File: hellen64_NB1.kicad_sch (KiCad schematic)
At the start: 192 parts, among them J1 USB_B_Mini, J11 Conn_01x01, J13 Conn_01x01, J14 Conn_01x01, J15 Conn_01x01, J16 Conn_01x01, J17 Conn_01x01, J19 Conn_01x01, J2 Conn_01x05_Male, J20 Conn_01x01, J21 Conn_01x01, J22 Conn_01x01, J24 Conn_01x01, J25 AudioJack3_SwitchTR, J27 Conn_01x06, J3 MiniFit, J4 Conn_02x12_Odd_Even, J5 USB_B, J6 ETB, M1 Module-input-0.1, M10 Module-power12-0.2, M11 Module-power5-0.2, M12 Module-wbo-0.2, M13 Module-can-0.1, M2 Module-ign8-0.1, M3 Module-mcu144-0.5, M4 Module-sd-0.1, M5 Module-output-0.2, M6 Module-dinput4-0.1, M7 Module-stlink-0.1, M8 Module-can-0.1, M9 Module-knock-0.1, P1 Pad, P10 Pad, P11 Pad, P12 Pad, P13 Pad, P14 Pad, P15 Pad, P17 Pad, P18 Pad, P19 Pad, P2 178780-1, P20 Pad, P22 Pad, P23 Pad, P24 Pad, P25 Pad, P28 Pad, P29 Pad, P30 Pad, P31 Pad, P32 Pad, P38 Pad, P4 Pad, P43 Pad, P44 Pad, P47 Pad, P48 Pad, P49 Pad, P5 Pad, P50 Pad, P51 Pad, P52 Pad, P53 Pad, P55 Pad, P56 Pad, P6 Pad, P7 Pad, P8 Pad, P9 Pad, U1 LIS2DW12TR, U2 MPX4_MAP, U3 MCP6002-xSN, U4 LPS25HB, U5 L6205PD

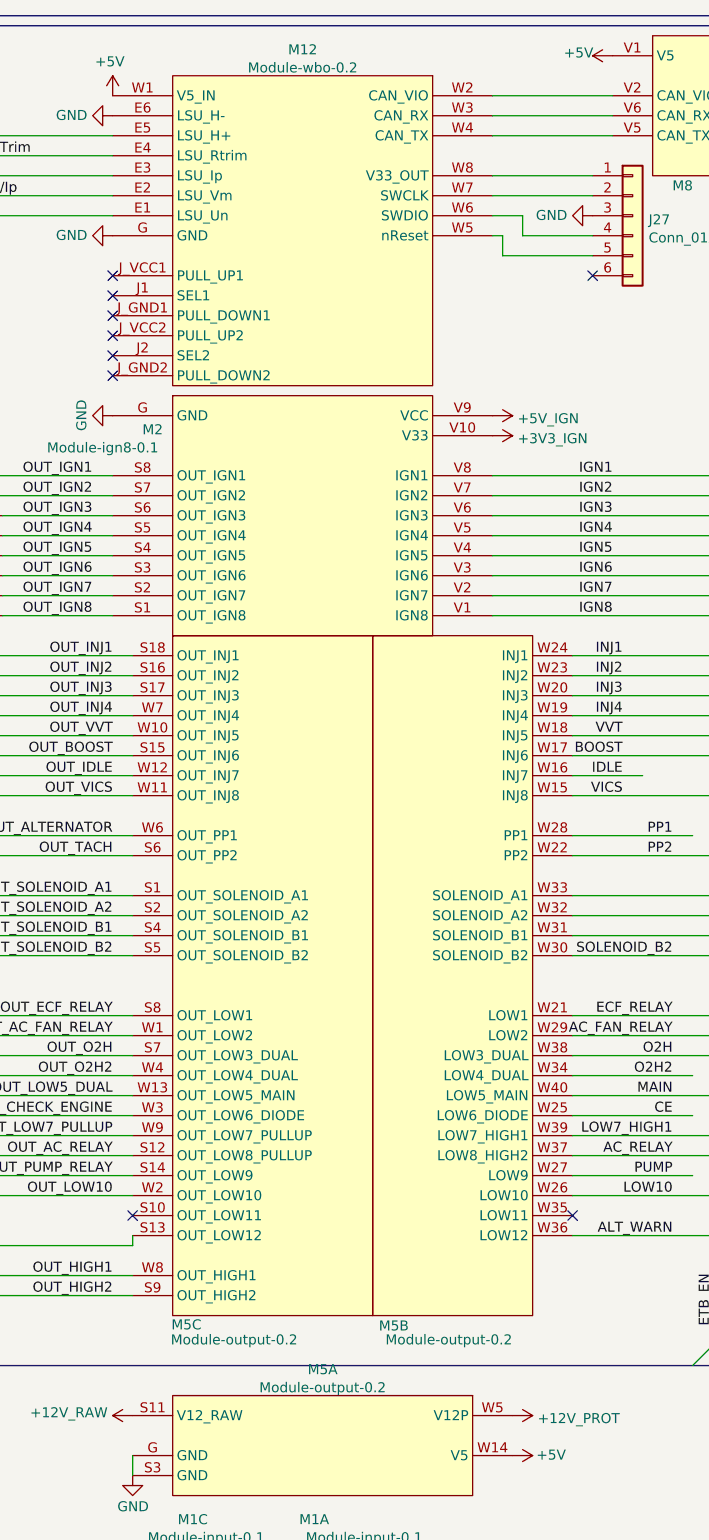
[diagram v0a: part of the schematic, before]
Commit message: update to output-0.3 and wbo-0.3
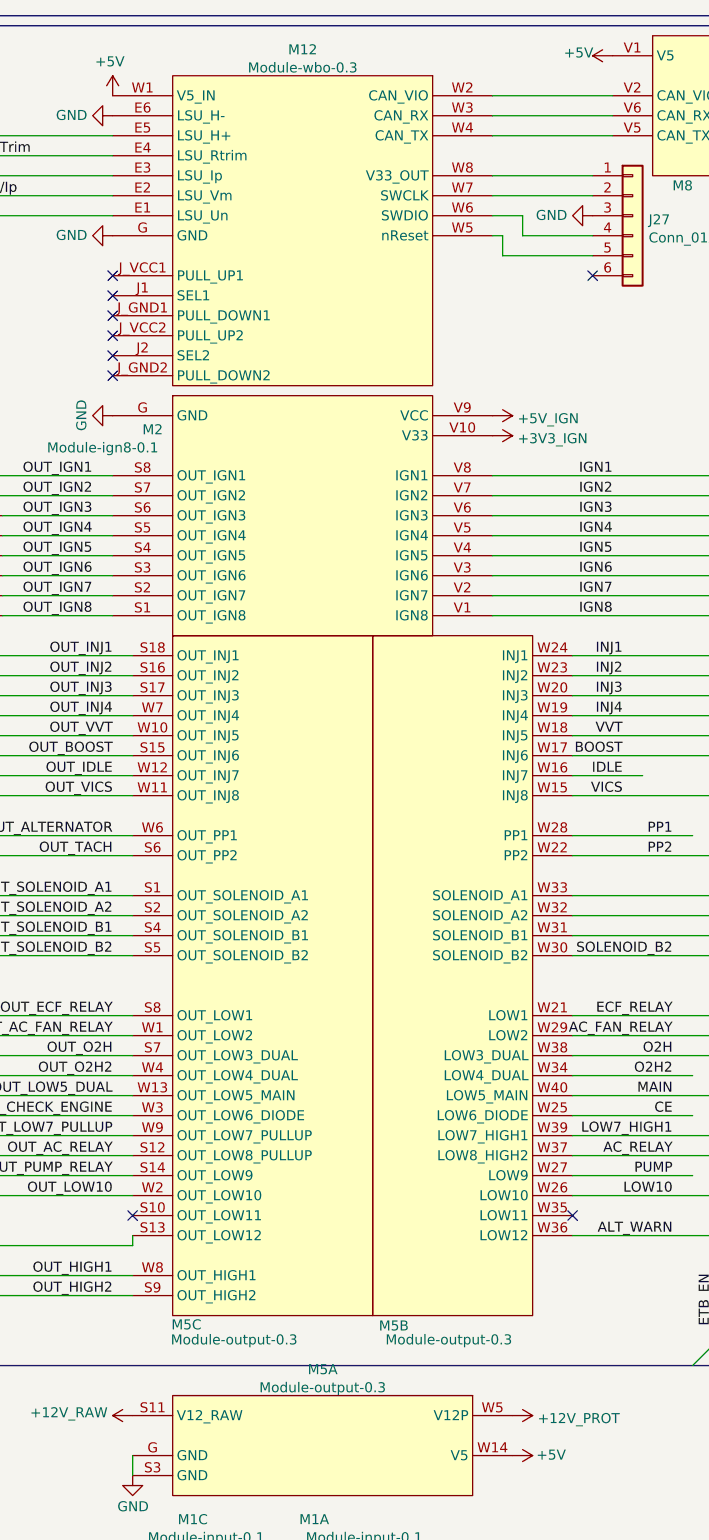
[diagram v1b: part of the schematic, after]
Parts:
- M11: footprint hellen-one-power5-0.1:power5 -> hellen-one-power5-0.2:power5; symbol hellen-one-power5-0.1:Module-power5-0.1 -> hellen-one-power5-0.2:Module-power5-0.2
- M12: value Module-wbo-0.2 -> Module-wbo-0.3; footprint hellen-one-wbo-0.2:wbo -> hellen-one-wbo-0.3:wbo; symbol hellen-one-wbo-0.2:Module-wbo-0.2 -> hellen-one-wbo-0.3:Module-wbo-0.3
- M3: footprint hellen-one-mcu-0.3:mcu -> hellen-one-mcu-0.5:mcu; symbol hellen-one-mcu-0.3:Module-mcu-0.3 -> hellen-one-mcu-0.5:Module-mcu-0.5
- M5: value Module-output-0.2 -> Module-output-0.3; footprint hellen-one-output-0.2:output -> hellen-one-output-0.3:output; symbol hellen-one-output-0.2:Module-output-0.2 -> hellen-one-output-0.3:Module-output-0.3
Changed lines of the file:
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@@
     (pin "9")
   )
-  (symbol (lib_id "hellen-one-output-0.2:Module-output-0.2") (at 314.96 187.96 0) (unit 1)
+  (symbol (lib_id "hellen-one-output-0.3:Module-output-0.3") (at 314.96 187.96 0) (unit 1)
     (in_bom yes) (on_board yes) (fields_autoplaced)
     (property "Reference" "M5" (id 0) (at 334.01 184.6538 0))
-    (property "Value" "Module-output-0.2" (id 1) (at 334.01 186.9525 0))
-    (property "Footprint" "hellen-one-output-0.2:output" (id 2) (at 314.96 187.96 0)
+    (property "Value" "Module-output-0.3" (id 1) (at 334.01 186.9525 0))
+    (property "Footprint" "hellen-one-output-0.3:output" (id 2) (at 314.96 187.96 0)
       (effects (font (size 1.27 1.27)) hide)
     )
@@
     (pin "W4")
   )
-  (symbol (lib_id "hellen-one-mcu-0.3:Module-mcu-0.3") (at 455.93 218.44 0) (unit 4)
+  (symbol (lib_id "hellen-one-mcu-0.5:Module-mcu-0.5") (at 455.93 218.44 0) (unit 4)
     (in_bom yes) (on_board yes) (fields_autoplaced)
     (property "Reference" "M3" (id 0) (at 473.71 215.1338 0))
     (property "Value" "Module-mcu144-0.5" (id 1) (at 473.71 217.4325 0))
-    (property "Footprint" "hellen-one-mcu-0.3:mcu" (id 2) (at 455.93 218.44 0)
+    (property "Footprint" "hellen-one-mcu-0.5:mcu" (id 2) (at 455.93 218.44 0)
       (effects (font (size 1.27 1.27)) hide)
     )
@@
     (pin "V5")
   )
-  (symbol (lib_id "hellen-one-power5-0.1:Module-power5-0.1") (at 107.95 257.81 0) (unit 1)
+  (symbol (lib_id "hellen-one-power5-0.2:Module-power5-0.2") (at 107.95 257.81 0) (unit 1)
     (in_bom yes) (on_board yes) (fields_autoplaced)
     (property "Reference" "M11" (id 0) (at 124.46 254.5038 0))
     (property "Value" "Module-power5-0.2" (id 1) (at 124.46 256.8025 0))
-    (property "Footprint" "hellen-one-power5-0.1:power5" (id 2) (at 107.95 257.81 0)
+    (property "Footprint" "hellen-one-power5-0.2:power5" (id 2) (at 107.95 257.81 0)
       (effects (font (size 1.27 1.27)) hide)
     )
@@
     (pin "J9")
   )
-  (symbol (lib_id "hellen-one-wbo-0.2:Module-wbo-0.2") (at 347.98 20.32 0) (mirror y) (unit 1)
+  (symbol (lib_id "hellen-one-wbo-0.3:Module-wbo-0.3") (at 347.98 20.32 0) (mirror y) (unit 1)
     (in_bom yes) (on_board yes) (fields_autoplaced)
     (property "Reference" "M12" (id 0) (at 331.47 17.0138 0))
-    (property "Value" "Module-wbo-0.2" (id 1) (at 331.47 19.3125 0))
-    (property "Footprint" "hellen-one-wbo-0.2:wbo" (id 2) (at 322.58 19.05 0)
+    (property "Value" "Module-wbo-0.3" (id 1) (at 331.47 19.3125 0))
+    (property "Footprint" "hellen-one-wbo-0.3:wbo" (id 2) (at 322.58 19.05 0)
       (effects (font (size 1.27 1.27)) hide)
     )
@@
     (pin "W8")
   )
-  (symbol (lib_id "hellen-one-mcu-0.3:Module-mcu-0.3") (at 420.37 207.01 0) (unit 3)
+  (symbol (lib_id "hellen-one-mcu-0.5:Module-mcu-0.5") (at 420.37 207.01 0) (unit 3)
     (in_bom yes) (on_board yes)
     (property "Reference" "M3" (id 0) (at 418.4651 203.7091 0)
@@
       (effects (font (size 1.27 1.27)) (justify left))
     )
-    (property "Footprint" "hellen-one-mcu-0.3:mcu" (id 2) (at 420.37 207.01 0)
+    (property "Footprint" "hellen-one-mcu-0.5:mcu" (id 2) (at 420.37 207.01 0)
       (effects (font (size 1.27 1.27)) hide)
     )
@@
     (pin "S9")
   )
-  (symbol (lib_id "hellen-one-output-0.2:Module-output-0.2") (at 360.68 91.44 0) (mirror y) (unit 2)
+  (symbol (lib_id "hellen-one-output-0.3:Module-output-0.3") (at 360.68 91.44 0) (mirror y) (unit 2)
     (in_bom yes) (on_board yes)
     (property "Reference" "M5" (id 0) (at 343.0475 179.1027 0))
-    (property "Value" "Module-output-0.2" (id 1) (at 350.0359 180.8703 0))
-    (property "Footprint" "hellen-one-output-0.2:output" (id 2) (at 360.68 91.44 0)
+    (property "Value" "Module-output-0.3" (id 1) (at 350.0359 180.8703 0))
+    (property "Footprint" "hellen-one-output-0.3:output" (id 2) (at 360.68 91.44 0)
       (effects (font (size 1.27 1.27)) hide)
     )
@@
     (pin "W40")
   )
-  (symbol (lib_id "hellen-one-mcu-0.3:Module-mcu-0.3") (at 435.61 68.58 0) (mirror y) (unit 2)
+  (symbol (lib_id "hellen-one-mcu-0.5:Module-mcu-0.5") (at 435.61 68.58 0) (mirror y) (unit 2)
     (in_bom yes) (on_board yes)
     (property "Reference" "M3" (id 0) (at 418.4651 65.2791 0)
@@
       (effects (font (size 1.27 1.27)) (justify right))
     )
-    (property "Footprint" "hellen-one-mcu-0.3:mcu" (id 2) (at 435.61 68.58 0)
+    (property "Footprint" "hellen-one-mcu-0.5:mcu" (id 2) (at 435.61 68.58 0)
       (effects (font (size 1.27 1.27)) hide)
     )
@@
     (pin "W8")
   )
-  (symbol (lib_id "hellen-one-mcu-0.3:Module-mcu-0.3") (at 435.61 68.58 0) (unit 1)
+  (symbol (lib_id "hellen-one-mcu-0.5:Module-mcu-0.5") (at 435.61 68.58 0) (unit 1)
     (in_bom yes) (on_board yes)
     (property "Reference" "M3" (id 0) (at 445.9605 65.2738 0))
     (property "Value" "Module-mcu144-0.5" (id 1) (at 451.0405 67.5725 0))
-    (property "Footprint" "hellen-one-mcu-0.3:mcu" (id 2) (at 435.61 68.58 0)
+    (property "Footprint" "hellen-one-mcu-0.5:mcu" (id 2) (at 435.61 68.58 0)
       (effects (font (size 1.27 1.27)) hide)
     )
@@
     (pin "N9")
   )
-  (symbol (lib_id "hellen-one-output-0.2:Module-output-0.2") (at 340.36 91.44 0) (mirror y) (unit 3)
+  (symbol (lib_id "hellen-one-output-0.3:Module-output-0.3") (at 340.36 91.44 0) (mirror y) (unit 3)
     (in_bom yes) (on_board yes)
     (property "Reference" "M5" (id 0) (at 314.7932 178.9645 0)
       (effects (font (size 1.27 1.27)) (justify right))
     )
-    (property "Value" "Module-output-0.2" (id 1) (at 314.7141 180.8756 0)
+    (property "Value" "Module-output-0.3" (id 1) (at 314.7141 180.8756 0)
       (effects (font (size 1.27 1.27)) (justify right))
     )
-    (property "Footprint" "hellen-one-output-0.2:output" (id 2) (at 340.36 91.44 0)
+    (property "Footprint" "hellen-one-output-0.3:output" (id 2) (at 340.36 91.44 0)
       (effects (font (size 1.27 1.27)) hide)
     )
@@
     )
     (path "/a6bf355d-1d5f-4e79-8e3f-45e3bddf3ceb"
-      (reference "M3") (unit 1) (value "Module-mcu144-0.5") (footprint "hellen-one-mcu-0.3:mcu")
+      (reference "M3") (unit 1) (value "Module-mcu144-0.5") (footprint "hellen-one-mcu-0.5:mcu")
     )
     (path "/915d735b-9683-4d94-8b0d-1fa27ebac489"
-      (reference "M3") (unit 2) (value "Module-mcu144-0.5") (footprint "hellen-one-mcu-0.3:mcu")
+      (reference "M3") (unit 2) (value "Module-mcu144-0.5") (footprint "hellen-one-mcu-0.5:mcu")
     )
     (path "/5f1c7f30-e456-4e5e-847b-c87579bb1a4c"
-      (reference "M3") (unit 3) (value "Module-mcu144-0.5") (footprint "hellen-one-mcu-0.3:mcu")
+      (reference "M3") (unit 3) (value "Module-mcu144-0.5") (footprint "hellen-one-mcu-0.5:mcu")
     )
     (path "/a7d95f89-5755-415c-ab05-3cba0bcc1e6a"
-      (reference "M3") (unit 4) (value "Module-mcu144-0.5") (footprint "hellen-one-mcu-0.3:mcu")
+      (reference "M3") (unit 4) (value "Module-mcu144-0.5") (footprint "hellen-one-mcu-0.5:mcu")
     )
     (path "/46c92d79-ab77-4cea-933a-f95fdcee2757"
@@
     )
     (path "/0daa1d7b-dc4e-4925-8d2c-7394a8bbb0e2"
-      (reference "M5") (unit 1) (value "Module-output-0.2") (footprint "hellen-one-output-0.2:output")
+      (reference "M5") (unit 1) (value "Module-output-0.3") (footprint "hellen-one-output-0.3:output")
     )
     (path "/229bfd16-421d-49a0-a382-7d5056ead6a8"
-      (reference "M5") (unit 2) (value "Module-output-0.2") (footprint "hellen-one-output-0.2:output")
+      (reference "M5") (unit 2) (value "Module-output-0.3") (footprint "hellen-one-output-0.3:output")
     )
     (path "/808ed398-2b6d-4dc7-971d-699409b9d7b5"
-      (reference "M5") (unit 3) (value "Module-output-0.2") (footprint "hellen-one-output-0.2:output")
+      (reference "M5") (unit 3) (value "Module-output-0.3") (footprint "hellen-one-output-0.3:output")
     )
     (path "/be038c97-a47c-4a31-8977-1994fd78eb34"
@@
     )
     (path "/ecf48ddf-8d02-4570-8ae6-b2411fa17b9e"
-      (reference "M11") (unit 1) (value "Module-power5-0.2") (footprint "hellen-one-power5-0.1:power5")
+      (reference "M11") (unit 1) (value "Module-power5-0.2") (footprint "hellen-one-power5-0.2:power5")
     )
     (path "/624f7764-dafb-44b4-808f-9b43af24ec78"
-      (reference "M12") (unit 1) (value "Module-wbo-0.2") (footprint "hellen-one-wbo-0.2:wbo")
+      (reference "M12") (unit 1) (value "Module-wbo-0.3") (footprint "hellen-one-wbo-0.3:wbo")
     )
     (path "/9f52c856-b504-4fdc-ad5e-307e12a42829"

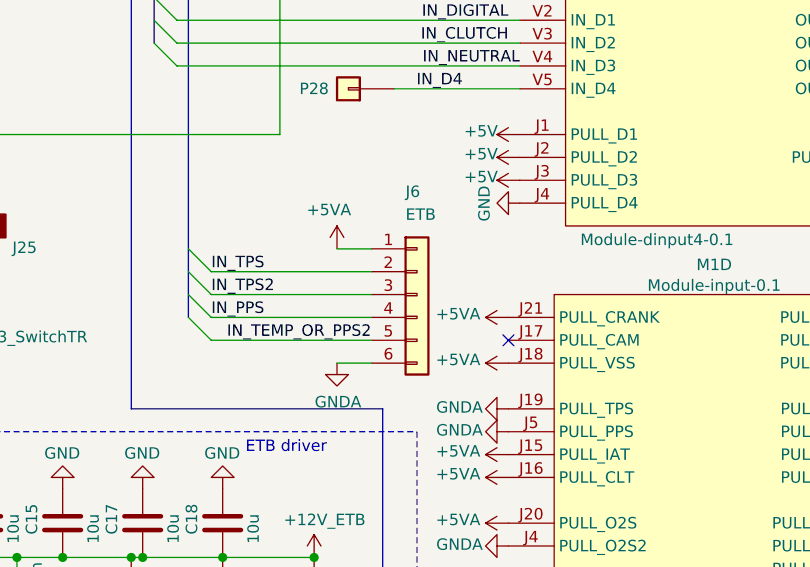
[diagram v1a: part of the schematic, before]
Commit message: etb connector 6pin->8pin
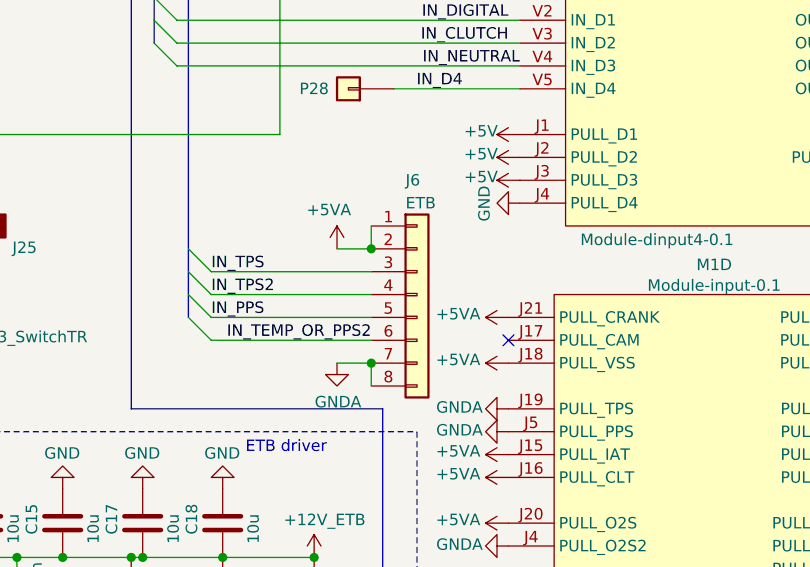
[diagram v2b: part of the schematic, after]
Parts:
- removed J6: ETB, hellen-one-common:PinHeader_1x06_P2.54mm_Vertical, symbol Connector_Generic:Conn_01x06
- added J6: ETB, hellen-one-common:PinHeader_1x08_P2.54mm_Vertical, symbol Connector_Generic:Conn_01x08
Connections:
- net +5VA: now also J6.1 (Pin_1), J6.2 (Pin_2)
- net GND: now also J6.7 (Pin_7), J6.8 (Pin_8)
- net IN_PPS: now also J6.5 (Pin_5)
- net IN_TEMP_OR_PPS2: now also J6.6 (Pin_6)
- net IN_TPS: now also J6.3 (Pin_3)
- net IN_TPS2: now also J6.4 (Pin_4)
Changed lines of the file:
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@@
   (junction (at 283.21 285.75) (diameter 1.016) (color 0 0 0 0))
   (junction (at 287.02 353.06) (diameter 1.016) (color 0 0 0 0))
+  (junction (at 293.37 318.77) (diameter 1.016) (color 0 0 0 0))
+  (junction (at 293.37 331.47) (diameter 1.016) (color 0 0 0 0))
   (junction (at 311.15 389.89) (diameter 1.016) (color 0 0 0 0))
   (junction (at 311.15 392.43) (diameter 1.016) (color 0 0 0 0))
@@
     (stroke (width 0) (type solid) (color 0 0 0 0))
   )
+  (wire (pts (xy 293.37 316.23) (xy 293.37 318.77))
+    (stroke (width 0) (type solid) (color 0 0 0 0))
+  )
   (wire (pts (xy 293.37 318.77) (xy 289.56 318.77))
     (stroke (width 0) (type solid) (color 0 0 0 0))
@@
     (stroke (width 0) (type solid) (color 0 0 0 0))
   )
+  (wire (pts (xy 293.37 331.47) (xy 293.37 334.01))
+    (stroke (width 0) (type solid) (color 0 0 0 0))
+  )
   (wire (pts (xy 294.64 245.11) (xy 309.88 245.11))
     (stroke (width 0) (type solid) (color 0 0 0 0))
@@
     (pin "2")
   )
-  (symbol (lib_id "Connector_Generic:Conn_01x06") (at 298.45 323.85 0) (unit 1)
-    (in_bom yes) (on_board yes)
-    (property "Reference" "J6" (id 0) (at 297.18 312.4199 0)
-      (effects (font (size 1.27 1.27)) (justify left))
-    )
-    (property "Value" "ETB" (id 1) (at 297.18 314.9599 0)
-      (effects (font (size 1.27 1.27)) (justify left))
-    )
-    (property "Footprint" "hellen-one-common:PinHeader_1x06_P2.54mm_Vertical" (id 2) (at 298.45 323.85 0)
-      (effects (font (size 1.27 1.27)) hide)
-    )
-    (property "Datasheet" "~" (id 3) (at 298.45 323.85 0)
-      (effects (font (size 1.27 1.27)) hide)
-    )
-    (property "LCSC" "C343639" (id 4) (at 298.45 323.85 0)
-      (effects (font (size 1.27 1.27)) hide)
-    )
-    (pin "1")
-    (pin "2")
-    (pin "3")
-    (pin "4")
-    (pin "5")
-    (pin "6")
-  )
   (symbol (lib_id "Connector_Generic:Conn_01x06") (at 373.38 38.1 0) (unit 1)
     (in_bom yes) (on_board yes) (fields_autoplaced)
@@
     (pin "2")
   )
+  (symbol (lib_id "Connector_Generic:Conn_01x08") (at 298.45 323.85 0) (unit 1)
+    (in_bom yes) (on_board yes)
+    (property "Reference" "J6" (id 0) (at 297.18 311.1499 0)
+      (effects (font (size 1.27 1.27)) (justify left))
+    )
+    (property "Value" "ETB" (id 1) (at 297.18 313.6899 0)
+      (effects (font (size 1.27 1.27)) (justify left))
+    )
+    (property "Footprint" "hellen-one-common:PinHeader_1x08_P2.54mm_Vertical" (id 2) (at 298.45 323.85 0)
+      (effects (font (size 1.27 1.27)) hide)
+    )
+    (property "Datasheet" "~" (id 3) (at 298.45 323.85 0)
+      (effects (font (size 1.27 1.27)) hide)
+    )
+    (property "LCSC" "C343639" (id 4) (at 298.45 323.85 0)
+      (effects (font (size 1.27 1.27)) hide)
+    )
+    (pin "1")
+    (pin "2")
+    (pin "3")
+    (pin "4")
+    (pin "5")
+    (pin "6")
+    (pin "7")
+    (pin "8")
+  )
   (symbol (lib_id "Amplifier_Operational:MCP6002-xSN") (at 193.04 304.8 0) (mirror x) (unit 2)
     (in_bom yes) (on_board yes) (fields_autoplaced)
@@
       (reference "J5") (unit 1) (value "USB_B") (footprint "hellen-one-common:USB_B")
     )
-    (path "/5afe1100-8c97-4555-be41-881acb241b5f"
-      (reference "J6") (unit 1) (value "ETB") (footprint "hellen-one-common:PinHeader_1x06_P2.54mm_Vertical")
+    (path "/9b2d5feb-f825-4b5d-9245-ed6143e67604"
+      (reference "J6") (unit 1) (value "ETB") (footprint "hellen-one-common:PinHeader_1x08_P2.54mm_Vertical")
     )
     (path "/c467b6a1-0ecf-4233-9937-9acba863c9f6"
